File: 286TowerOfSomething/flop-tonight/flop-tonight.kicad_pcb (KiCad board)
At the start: 2 copper layers, 23 parts, among them J1 Bus_ISA_8bit, J2 Conn_02x17_Odd_Even, U1 PC8477BV, U2 74ALS138, U3 74ALS138, Y1 24 MHz

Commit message: Some work on the flop-tonight layout
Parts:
- moved JP1 103.8 mm to (83.8, 74.9)
- moved C10 70.3 mm to (149.9, 114.3)
- moved C3 2.54 mm to (144.8, 91.4)
- moved C9 1.04 mm to (116.8, 77.2)
- moved C8 0.63 mm to (134.6, 76.8)
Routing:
- net +5V: track 9.53 -> 159.8 mm, vias 0 -> 2
- net Net-(J2-Pin_8): track 0.00 -> 94.6 mm, vias 0 -> 3
- net Net-(J2-Pin_6): track 0.00 -> 89.4 mm, vias 0 -> 3
- net /TC: track 0.00 -> 70.7 mm, vias 0 -> 1
- net Net-(J2-Pin_2): track 0.00 -> 68.3 mm, vias 0 -> 1
- net Net-(J2-Pin_34): track 0.00 -> 57.9 mm, vias 0 -> 1
- net /AEN: track 0.00 -> 53.4 mm, vias 0 -> 1
- net Net-(J2-Pin_30): track 0.00 -> 50.5 mm, vias 0 -> 1
- net Net-(J2-Pin_10): track 0.00 -> 50.2 mm, vias 0 -> 1
- net /IRQ6: track 0.00 -> 49.9 mm, vias 0 -> 1
- net /~{DACK2}: track 0.00 -> 47.5 mm
- net Net-(J2-Pin_12): track 0.00 -> 42.6 mm, vias 0 -> 1
- net Net-(J2-Pin_28): track 0.00 -> 42.2 mm, vias 0 -> 3
- net Net-(J2-Pin_14): track 0.00 -> 40.8 mm, vias 0 -> 1
- net Net-(J2-Pin_26): track 0.00 -> 40.1 mm, vias 0 -> 1
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- added copper zone on B.Cu, net GND
- added copper zone on F.Cu, net GND

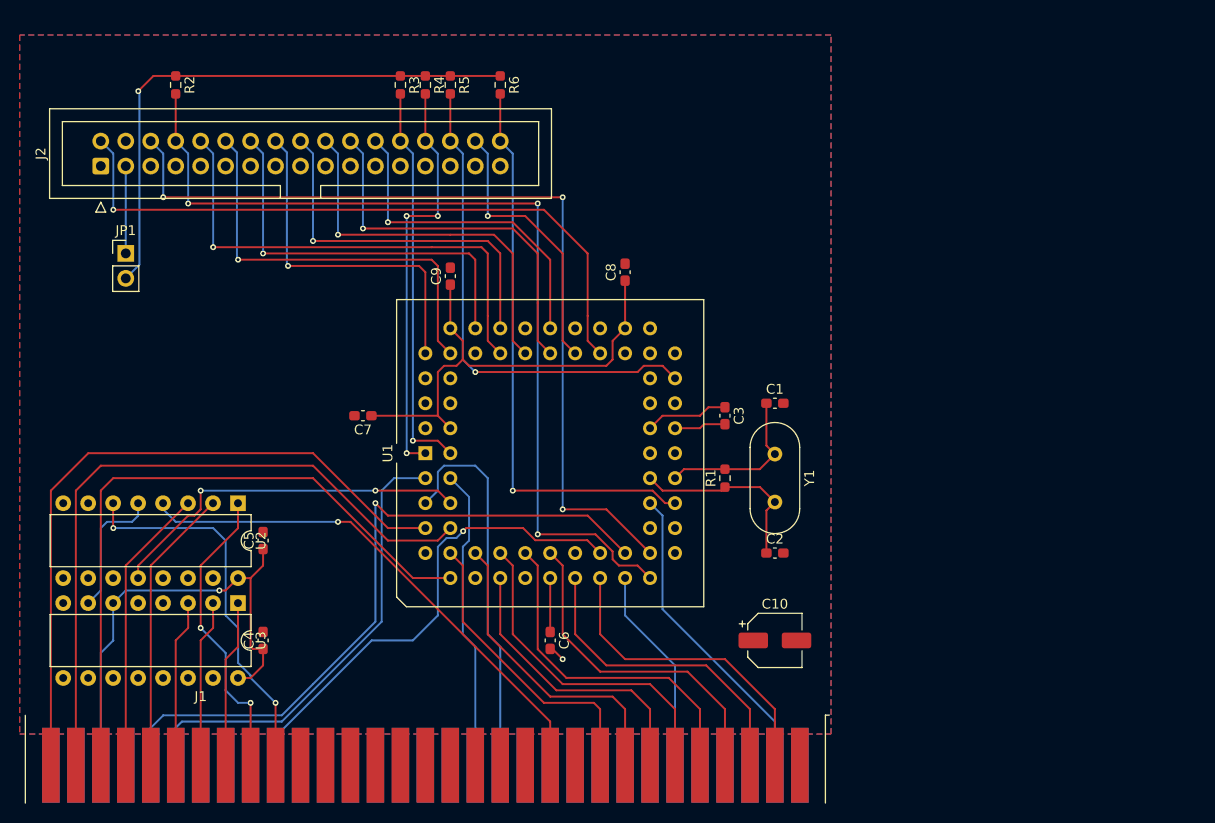
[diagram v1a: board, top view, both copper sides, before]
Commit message: Layout for Flop Tonight is complete. Needs adjustment to fit a bracket properly.
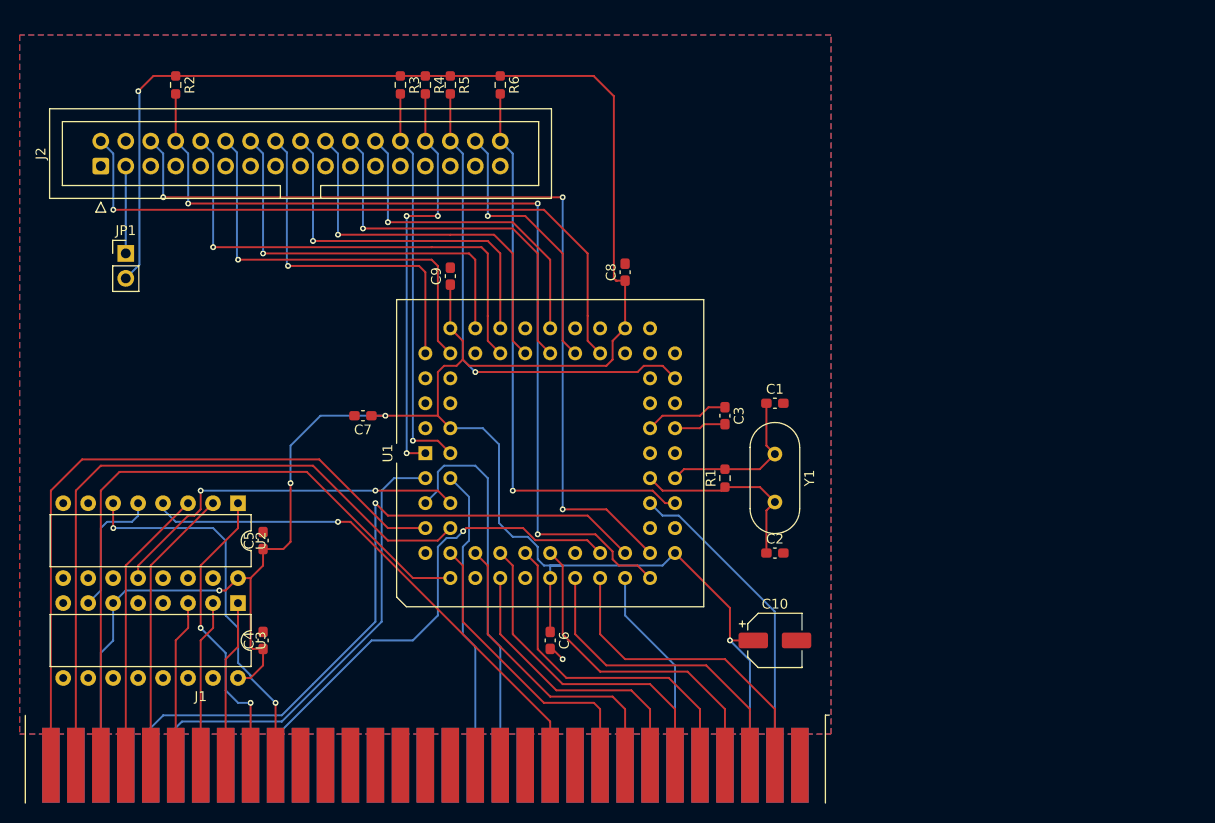
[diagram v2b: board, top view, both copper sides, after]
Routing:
- net +5V: track 159.8 -> 280.1 mm, vias 2 -> 5
- net /RESET: track 31.9 -> 32.9 mm
- net /A0: track 70.8 -> 70.2 mm
- net /A2: track 68.2 -> 68.8 mm
